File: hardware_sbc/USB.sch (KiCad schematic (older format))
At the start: 31 parts, among them J13 USB_C_Receptacle, U1 IMX8MM, U8 NX20P3483UK, U9 PTN5110NHQZ

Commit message: Clean up bom and add config for KiBoM
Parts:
- F1: Mfgr (none) -> Bourns
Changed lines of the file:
@@
 F 4 "SF-1206FP700-2CT-ND" V 8467 1850 50  0000 C CNN "Vendorpart"
 F 5 "SF-1206FP700-2" H 8600 1850 50  0001 C CNN "Part"
+F 6 "Bourns" H 8600 1850 50  0001 C CNN "Mfgr"
 	1    8600 1850
 	0    -1   1    0

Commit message: BOM and misc fixes for production of 0.9 boards
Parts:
- C162: Mfgrpart (none) -> C3216X5R1E476M160AC; Part C3216X5R1E476M160AC -> (none)
- C163, C165, C168, C174: Mfgrpart (none) -> GRM155R71E104KE14J; Part GRM155R71E104KE14J -> (none)
- C164, C169, C172: Mfgrpart (none) -> JMK107C6475MA-T; Part JMK107C6475MA-T -> (none)
- C166, C167: Mfgrpart (none) -> GRM033C80J224KE90D; Part GRM033C80J224KE90D -> (none)
- C170: Mfgrpart (none) -> GRM033R71C103KE14D; Part GRM033R71C103KE14D -> (none)
- C171: Mfgrpart (none) -> GRM033R71H102KA12J; Part GRM033R71H102KA12J -> (none)
- C173: Mfgrpart (none) -> GRM155C80J225ME95D; Part GRM155C80J225ME95D -> (none)
- D6, D7, D8, D9: Mfgrpart (none) -> ESD130B1W0201E6327XTSA1; Part ESD130B1W0201E6327XTSA1 -> (none)
- F1: Mfgrpart (none) -> SF-1206FP700-2; Part SF-1206FP700-2 -> (none)
- J13: Mfgr JAE -> GCT; Mfgrpart (none) -> 2073-USB4110-GF-A-1-ND; Part DX07S024JJ2R1300 -> (none); Vendorpart 670-2794-1-ND -> USB4110-GF-A
- R64, R65: Mfgrpart (none) -> RC0201FR-0730KL; Part RC0201FR-0730KL -> (none)
- R66, R69: Mfgrpart (none) -> RC0201FR-07200RL; Part RC0201FR-07200RL -> (none)
- R67, R68: Mfgrpart (none) -> RC0201JR-07100KL; Part RC0201JR-07100KL -> (none)
- R70: Mfgrpart (none) -> ERJ-1GNJ103C; Part ERJ-1GNJ103C -> (none)
- U1: Mfgrpart (none) -> MIMX8MM6CVTKZAA; Part MIMX8MM6CVTKZAA -> (none)
- U8: Mfgrpart (none) -> NX20P3483UK; Part NX20P3483UK -> (none)
- U9: Mfgrpart (none) -> PTN5110NHQZ; Part PTN5110NHQZ -> (none)

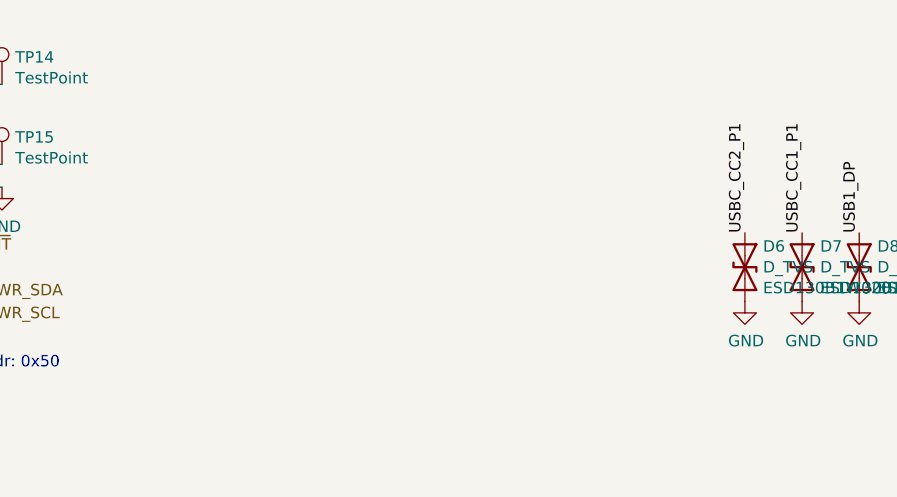
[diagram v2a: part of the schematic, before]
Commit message: Update BoM and add some errata notes for v0.9 builds moving forward
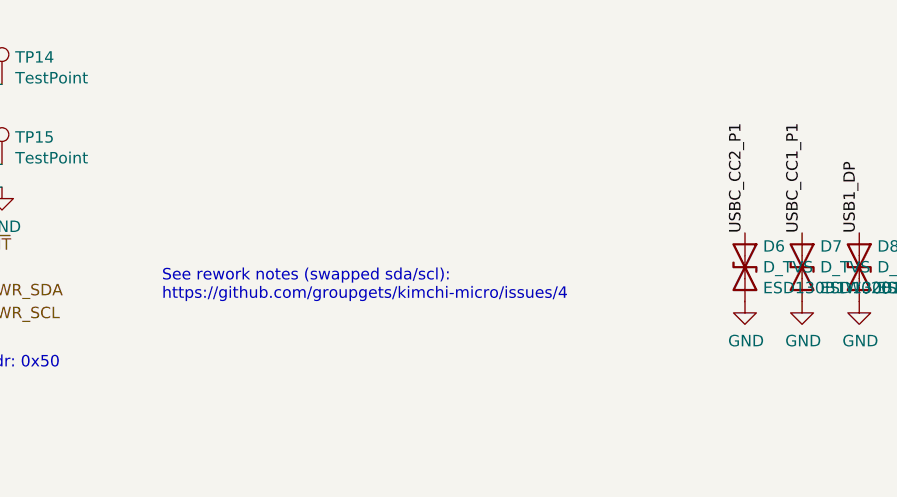
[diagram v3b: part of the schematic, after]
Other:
- note added: "See rework notes (swapped sda/scl):\nhttps://github.com/groupgets/kimchi-micro/issues/4"
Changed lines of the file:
@@
 	1    0    0    -1
 $EndComp
+Text Notes 9300 7950 0    50   ~ 0
+See rework notes (swapped sda/scl):\nhttps://github.com/groupgets/kimchi-micro/issues/4
 $EndSCHEMATC
